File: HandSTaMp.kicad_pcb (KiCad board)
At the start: 2 copper layers, 40.6 x 16.5 mm, 19 parts, among them J1 USB_C_Receptacle_USB2.0_16P, J2 SDI, J3 Pins, J4 ⏚, SW1 Row 0, Col+0, SW2 Row 0, Col+1, U2 PRTR5V0U2X, U4 CH32X035G8U6

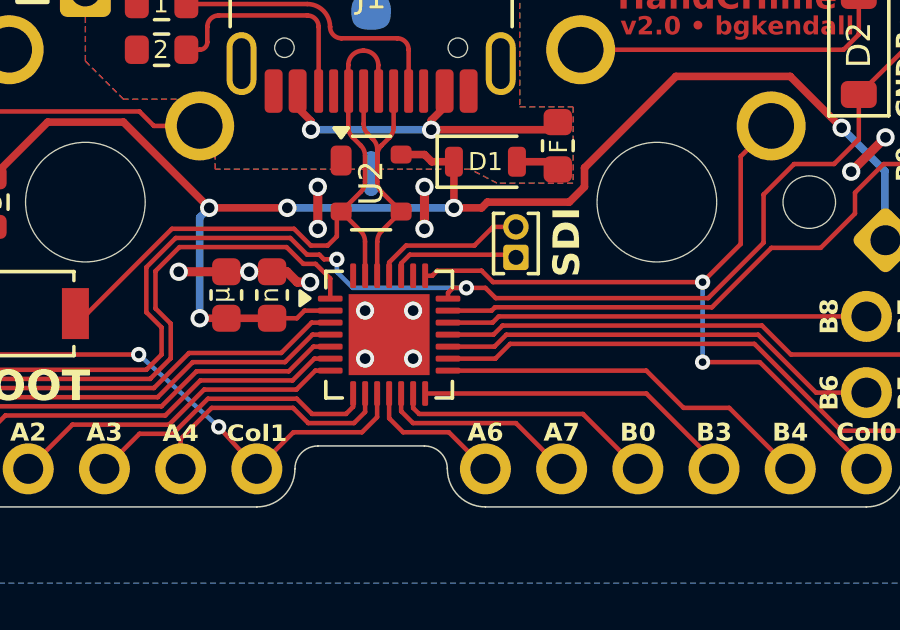
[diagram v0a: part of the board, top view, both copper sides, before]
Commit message: Adjust position of SDI connection
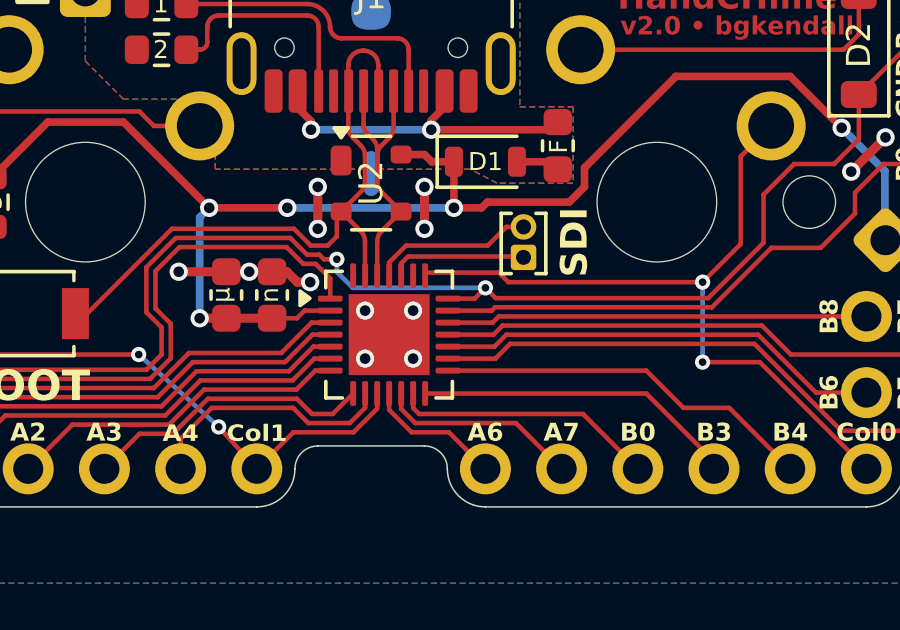
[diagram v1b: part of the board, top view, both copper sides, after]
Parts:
- moved J2 0.25 mm to (106.7, 52.1)
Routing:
- net R0: track 59.7 -> 60.2 mm

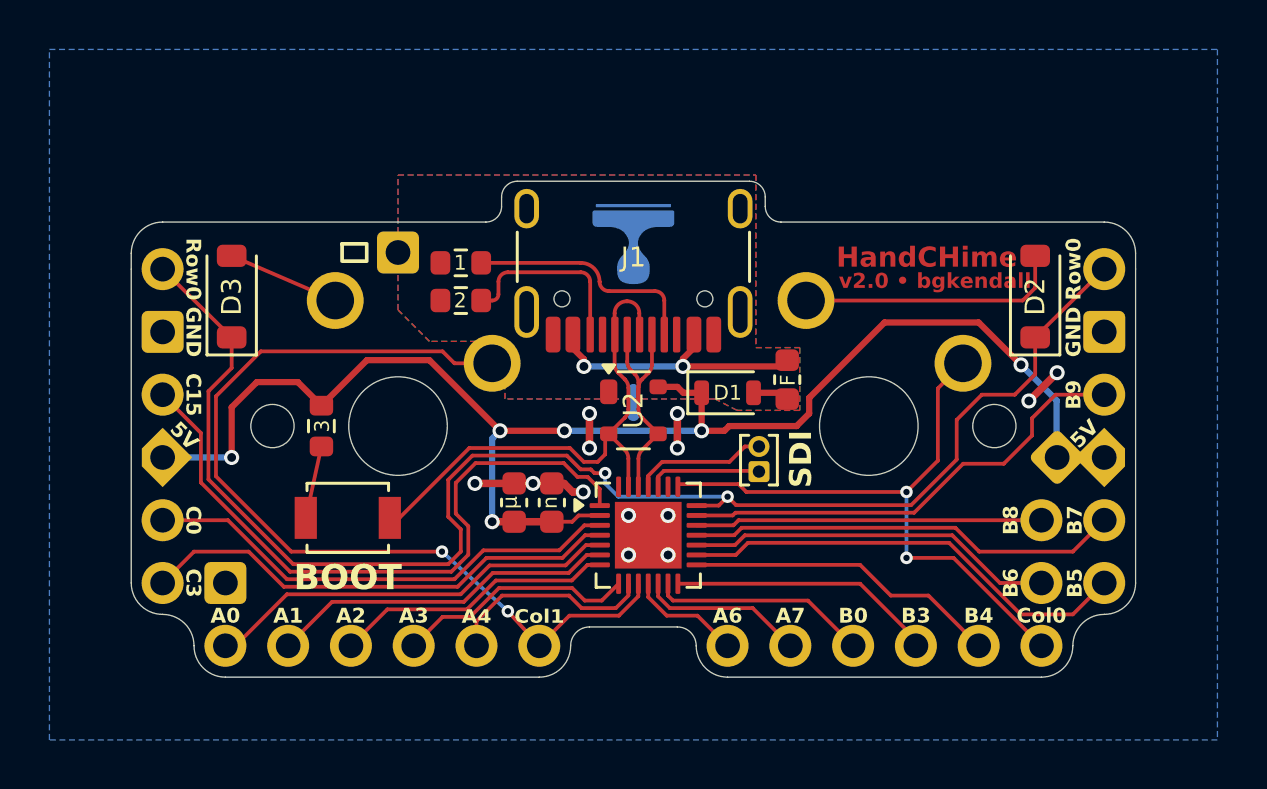
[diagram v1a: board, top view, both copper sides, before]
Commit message: Remove extra VCC connection
Since we don’t have a 3V3 pin any more, we probably don’t need a third 5V.
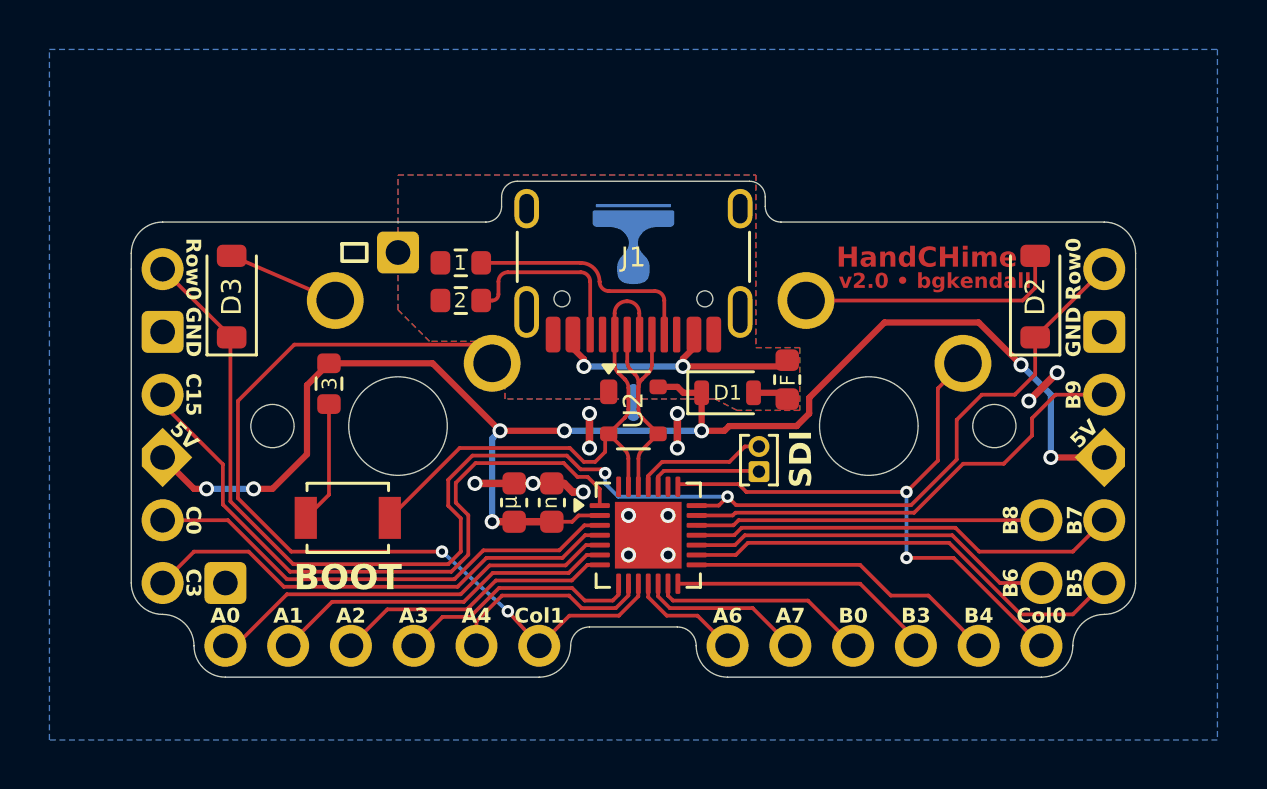
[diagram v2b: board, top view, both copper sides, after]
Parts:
- moved R3 1.74 mm to (89.3, 49.1)
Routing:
- net VCC: track 58.5 -> 61.6 mm, vias 6 -> 8
- net Net-(R3-Pad1): track 2.96 -> 5.12 mm
- net C1: track 36.9 -> 35.8 mm
- net R0: track 60.2 -> 59.5 mm

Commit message: Draft equal number of extra corner pins on each side
Pins need relabelling!
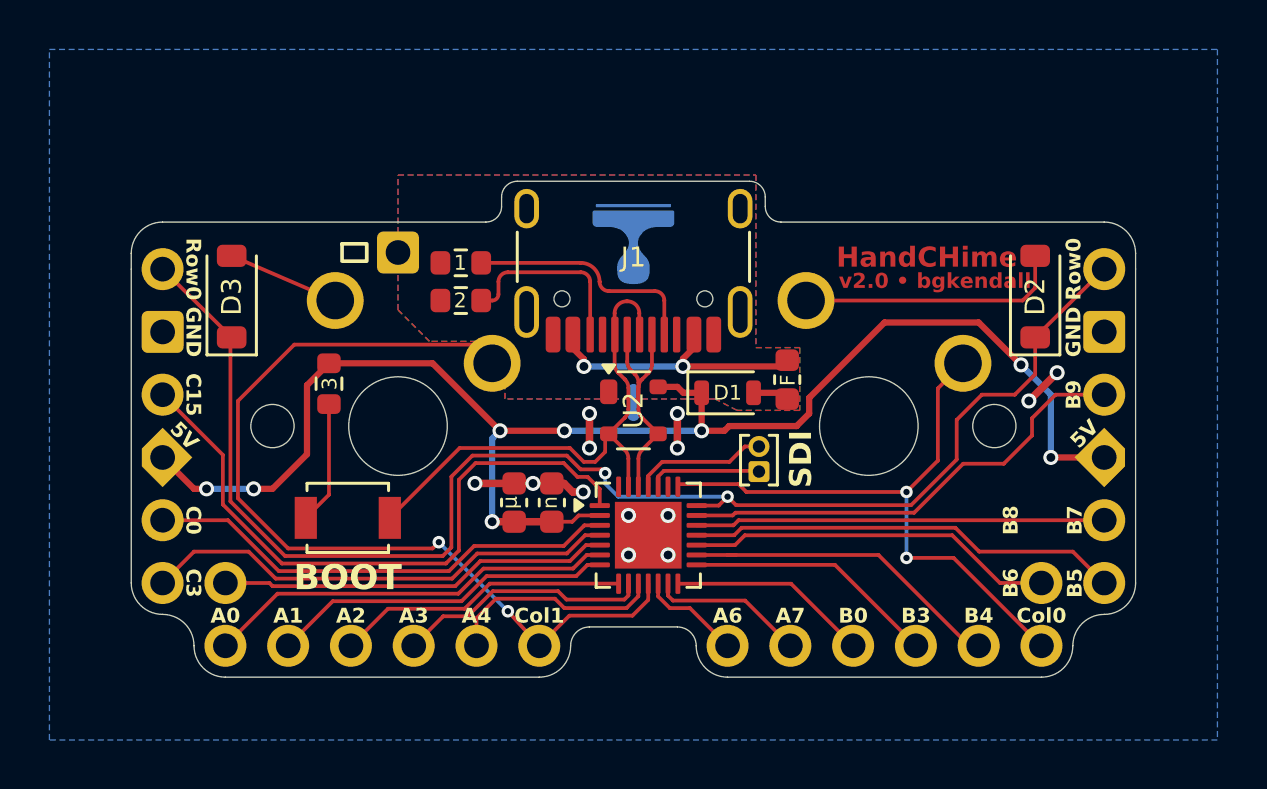
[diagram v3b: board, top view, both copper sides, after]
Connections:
- J3 pad 13: C1 -> PA6
- J3 pad 14: PA6 -> C1
- J3 pad 19: C0 -> PB5
- J3 pad 20: PB6 -> C0
- J3 pad 21: PB5 -> PB6
- J3 pad 22: PB8 -> PB7
- J3 pad 23: PB7 -> PB8
- U4 pad 10: C1 -> PA6
- U4 pad 11: PA6 -> C1
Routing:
- net PB5: track 18.4 -> 13.3 mm
- net PA6: track 4.74 -> 8.86 mm
- net PA1: track 14.1 -> 17.1 mm
- net PB3: track 10.8 -> 8.13 mm
- net PB8: track 14.0 -> 16.6 mm
- net PA2: track 11.4 -> 14.0 mm
- net PB0: track 8.81 -> 6.27 mm
- net PA7: track 6.69 -> 4.33 mm
- net PB4: track 12.8 -> 10.5 mm
- net PA3: track 10.0 -> 11.9 mm
- net PA4: track 8.47 -> 10.3 mm
- net PC15: track 27.2 -> 26.2 mm
- net R0: track 59.5 -> 58.5 mm
- net PA0: track 16.8 -> 15.9 mm
- net C1: track 35.8 -> 36.4 mm

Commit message: Fix pin assignments and labels
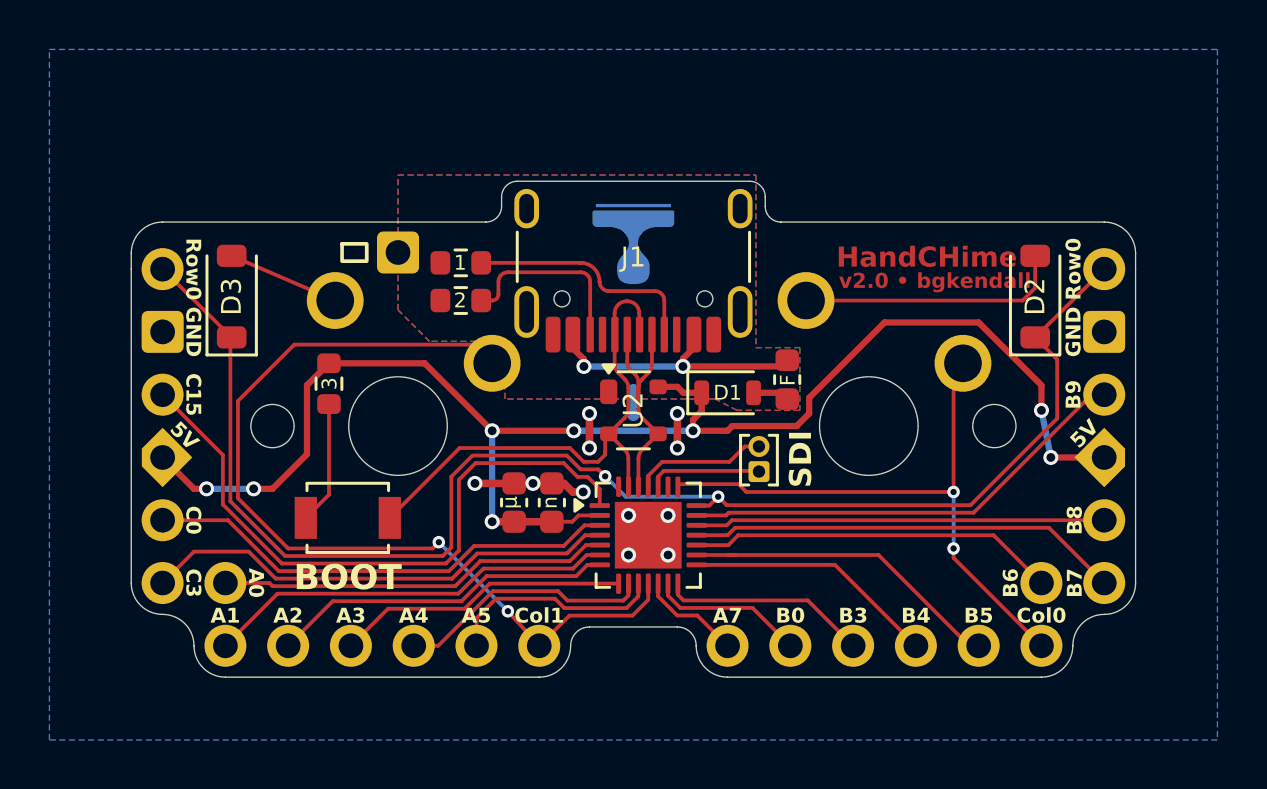
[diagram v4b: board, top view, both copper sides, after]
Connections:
- net C0 renamed Col0
- net C1 renamed Col1
- net PA6 renamed PA5
- net R0 renamed Row0
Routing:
- net GND: track 8.94 -> 7.32 mm, vias 13 -> 11
- net Col0: track 25.1 -> 24.3 mm
- net Row0: track 58.5 -> 59.2 mm

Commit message: Switch Row to PA3
This requires more trace crossings, but means that there isn’t a crossing under the MCU’s USB pads.
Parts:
- moved S3 0.76 mm to (89.3, 54.5)
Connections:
- J3 pad 10: PA2 -> PA1
- J3 pad 11: PA3 -> PA2
- J3 pad 5: PC15 -> PC14
- J3 pad 6: PC0 -> PC15
- J3 pad 8: PA0 -> PC0
- J3 pad 9: PA1 -> PA0
- U4 pad 21: Row0 -> Col0
- U4 pad 22: Col0 -> unconnected-(U4-PB11-Pad22)
- U4 pad 28: unconnected-(U4-PC14/CC1-Pad28) -> PC14
- U4 pad 8: PA3 -> Row0
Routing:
- net PC14: track 0.00 -> 27.0 mm
- net PA3: track 11.9 -> 0.00 mm
- net PC0: track 19.3 -> 16.1 mm
- net PA1: track 17.1 -> 14.1 mm
- net PC15: track 26.2 -> 23.2 mm
- net PA2: track 14.0 -> 11.4 mm
- net PA0: track 15.9 -> 17.2 mm
- net Row0: track 59.2 -> 60.5 mm, vias 2 -> 6
- net USB+: track 21.0 -> 21.8 mm
- net Col1: track 36.4 -> 37.1 mm
- net PB9: track 18.5 -> 19.1 mm
- net PB8: track 16.6 -> 17.1 mm
